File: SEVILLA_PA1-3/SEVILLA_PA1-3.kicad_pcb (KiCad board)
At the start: 2 copper layers, 64 x 46 mm, 10 parts, among them SW3 SW_SPST, SW4 SW_SPST, U1 HDSP-7401, U2 PIC16F84A-XXP, U3 HDSP-7401, Y1 4 MHz

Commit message: Refactor code structure and remove redundant sections for improved readability and maintainability
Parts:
- moved C2 44.5 mm to (161.0, 108.2), turned to 180 degrees
- moved U3 36.2 mm to (171.1, 91.0)
- moved U2 35.8 mm to (158.6, 101.6)
- moved U1 35.6 mm to (171.1, 105.6)
- moved SW4 33.1 mm to (118.5, 94.0)
- moved SW3 32.2 mm to (118.5, 80.0)
- moved R1 32.2 mm to (137.5, 77.5), turned to 90 degrees
- moved Y1 31.9 mm to (146.2, 83.5)
- moved R2 27.5 mm to (141.0, 98.0), turned to 180 degrees
- moved C1 22.3 mm to (146.0, 74.2)
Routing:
- net Net-(U1-F): track 41.6 -> 69.5 mm
- net GND: track 127.1 -> 152.1 mm
- net Net-(SW3-A): track 109.1 -> 88.9 mm
- net Net-(U1-E): track 61.3 -> 43.4 mm
- net Net-(U1-G): track 66.8 -> 49.3 mm
- net Net-(SW4-B): track 44.5 -> 59.4 mm
- net Net-(U2-RA3): track 55.0 -> 44.4 mm
- net Net-(U2-OSC2/CLKOUT): track 32.5 -> 24.9 mm
- net VCC: track 26.1 -> 19.5 mm
- net Net-(U1-C): track 27.0 -> 33.3 mm
- net Net-(U2-OSC1/CLKIN): track 30.8 -> 26.0 mm
- net Net-(U1-B): track 27.7 -> 24.1 mm
- net Net-(U2-TOCKI/RA4): track 26.7 -> 29.2 mm
- net Net-(U1-A): track 27.7 -> 25.4 mm
- net Net-(U1-D): track 31.9 -> 30.1 mm
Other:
- board size 64 x 46 mm -> 62 x 46 mm

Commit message: Refactor code structure for improved readability and maintainability
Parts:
- moved U1 1.76 mm to (171.5, 107.3)
- moved U2 1.76 mm to (159.0, 103.3)
- moved U3 1.76 mm to (171.5, 92.7)
- moved Y1 1.76 mm to (146.5, 85.2)
- moved SW3 1.76 mm to (118.9, 81.7)
- moved SW4 1.76 mm to (118.9, 95.7)
- moved C1 1.76 mm to (146.4, 75.9)
- moved C2 1.76 mm to (161.4, 110.0)
- moved R1 1.76 mm to (137.9, 79.2)
- moved R2 1.76 mm to (141.4, 99.7)
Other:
- board size 62 x 46 mm -> 100 x 50 mm
- board text removed: "100"
- board text removed: "20 pF"
- board text removed: "4 MHz"

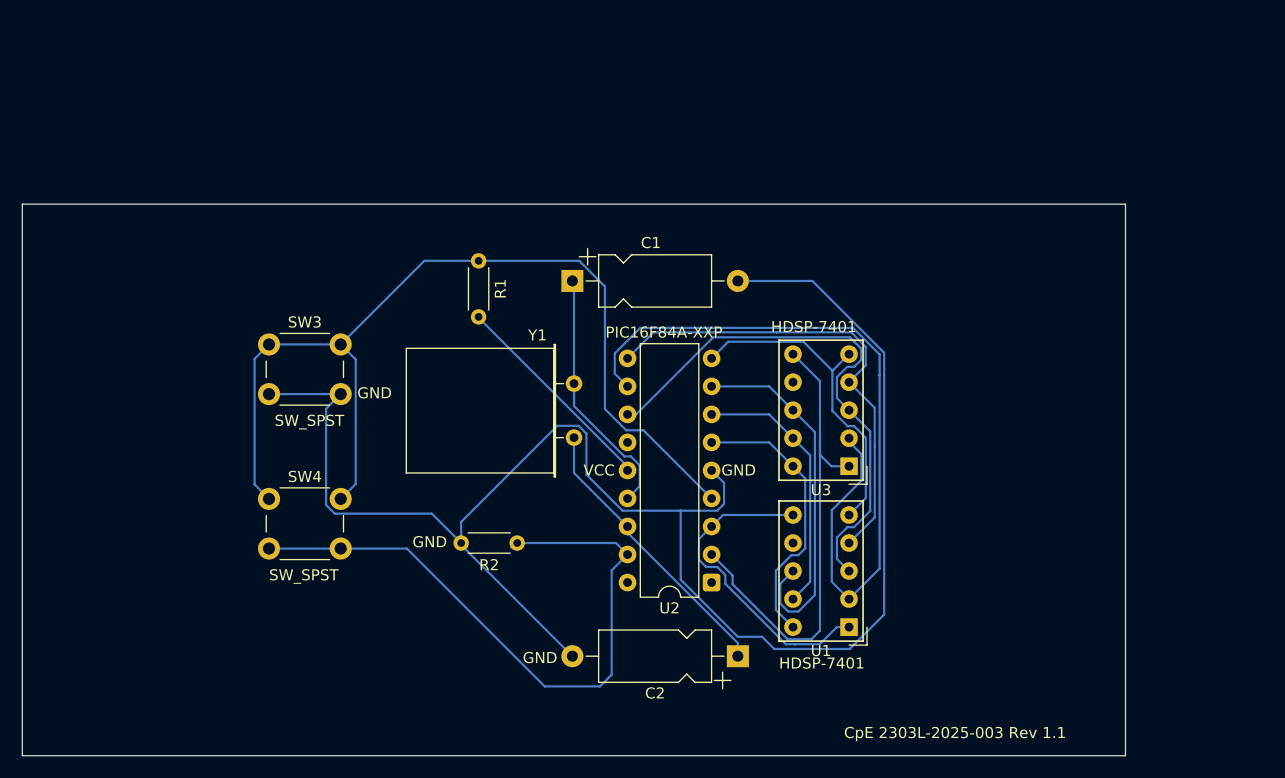
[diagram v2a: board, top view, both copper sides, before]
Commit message: Add lock file for PCB design with hostname and username information
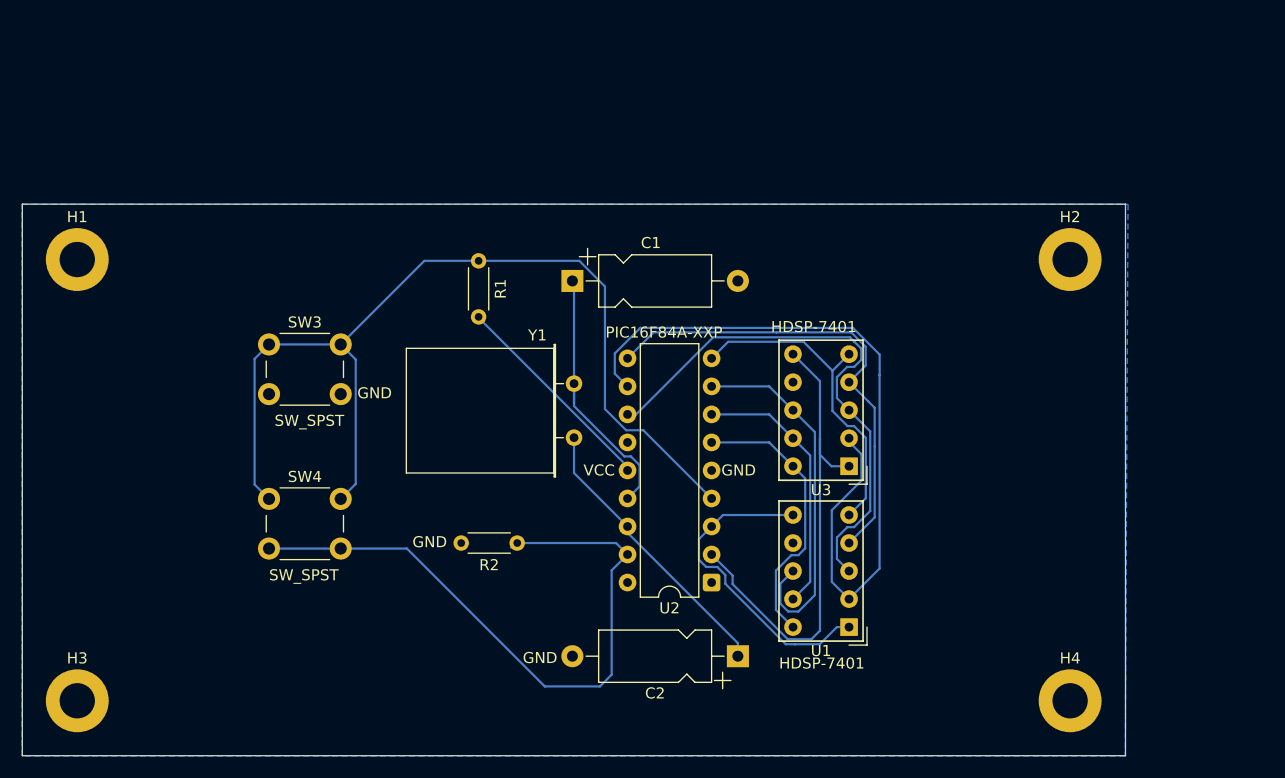
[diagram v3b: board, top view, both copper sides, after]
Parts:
- added H1: MountingHole, MountingHole:MountingHole_3.2mm_M3_ISO7380_Pad, F.Cu at (101.5, 74.0)
- added H2: MountingHole, MountingHole:MountingHole_3.2mm_M3_ISO7380_Pad, F.Cu at (191.5, 74.0)
- added H3: MountingHole, MountingHole:MountingHole_3.2mm_M3_ISO7380_Pad, F.Cu at (101.5, 114.0)
- added H4: MountingHole, MountingHole:MountingHole_3.2mm_M3_ISO7380_Pad, F.Cu at (191.5, 114.0)
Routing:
- net GND: track 152.1 -> 0.00 mm
- added copper zone on B.Cu, net GND
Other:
- board text added: "CpE 2303L-2025-003 Rev 1.2"
- board text removed: "CpE 2303L-2025-003 Rev 1.1"

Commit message: Refactor code structure for improved readability and maintainability
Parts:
- H1, H2, H3, H4: value MountingHole -> MountingHole_Pad
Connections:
- H1 pad 1: (no net) -> unconnected-(H1-Pad1)
- H2 pad 1: (no net) -> unconnected-(H2-Pad1)
- H3 pad 1: (no net) -> unconnected-(H3-Pad1)
- H4 pad 1: (no net) -> unconnected-(H4-Pad1)

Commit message: Refactor code structure and remove redundant sections for improved readability and maintainability
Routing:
- added copper zone on F.Cu, net GND
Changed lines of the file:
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@@
 		(net 1)
 		(net_name "GND")
-		(layer "B.Cu")
+		(layers "F.Cu" "B.Cu")
 		(hatch edge 0.5)
 		(connect_pads

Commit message: Refactor code structure and remove redundant sections for improved readability and maintainability
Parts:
- added J1: Conn_01x02, Connector_Molex:Molex_KK-254_AE-6410-02A_1x02_P2.54mm_Vertical, F.Cu at (143.6, 112.8)
- moved R2 47.0 mm to (185.8, 84.2), turned to -90 degrees
- moved C2 34.6 mm to (128.4, 99.6), turned to -90 degrees
- moved U1 33.0 mm to (146.6, 85.7), turned to 0 degrees
- moved U2 26.4 mm to (173.6, 81.3), turned to 0 degrees
- moved R1 26.4 mm to (140.8, 105.4)
- moved Y1 17.4 mm to (131.8, 94.5), turned to 180 degrees
- moved SW3 15.6 mm to (109.3, 94.1)
- moved SW4 15.4 mm to (109.3, 83.6)
- moved C1 14.9 mm to (131.6, 74.3)
- moved U3 12.9 mm to (160.0, 86.7), turned to 0 degrees
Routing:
- net Net-(U2-OSC1/CLKIN): track 26.0 -> 90.6 mm
- net Net-(U2-OSC2/CLKOUT): track 24.7 -> 74.4 mm
- net VCC: track 19.5 -> 61.4 mm
- net Net-(U1-G): track 49.3 -> 14.0 mm
- net Net-(U1-F): track 69.5 -> 39.2 mm
- net Net-(SW4-B): track 59.4 -> 87.5 mm
- net Net-(SW3-A): track 88.9 -> 104.0 mm
- net Net-(U2-TOCKI/RA4): track 29.2 -> 43.9 mm
- net Net-(U2-RA3): track 44.4 -> 30.0 mm
- net Net-(U1-C): track 33.3 -> 25.5 mm
- net Net-(U1-E): track 43.4 -> 38.2 mm
- net Net-(U1-B): track 24.1 -> 25.5 mm
- net Net-(U1-D): track 30.1 -> 29.5 mm
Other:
- board text removed: "VCC"

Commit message: Implement code changes to enhance functionality and improve performance
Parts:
- moved U1 15.9 mm to (155.0, 99.2)
- moved U3 7.68 mm to (155.4, 80.6)
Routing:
- net Net-(U1-F): track 39.2 -> 19.7 mm
- net Net-(SW3-A): track 104.0 -> 121.8 mm
- net Net-(U1-E): track 38.2 -> 55.2 mm
- net Net-(U1-G): track 14.0 -> 29.3 mm
- net Net-(U1-A): track 25.5 -> 39.4 mm
- net Net-(U1-D): track 29.5 -> 43.3 mm
- net Net-(U2-TOCKI/RA4): track 43.9 -> 32.4 mm
- net Net-(U1-C): track 25.5 -> 35.4 mm
- net Net-(U2-RA3): track 30.0 -> 20.8 mm
- net Net-(U2-OSC1/CLKIN): track 90.6 -> 98.7 mm
- net Net-(U1-B): track 25.5 -> 31.5 mm
- net VCC: track 61.4 -> 63.8 mm
- net Net-(U2-OSC2/CLKOUT): track 74.4 -> 75.0 mm

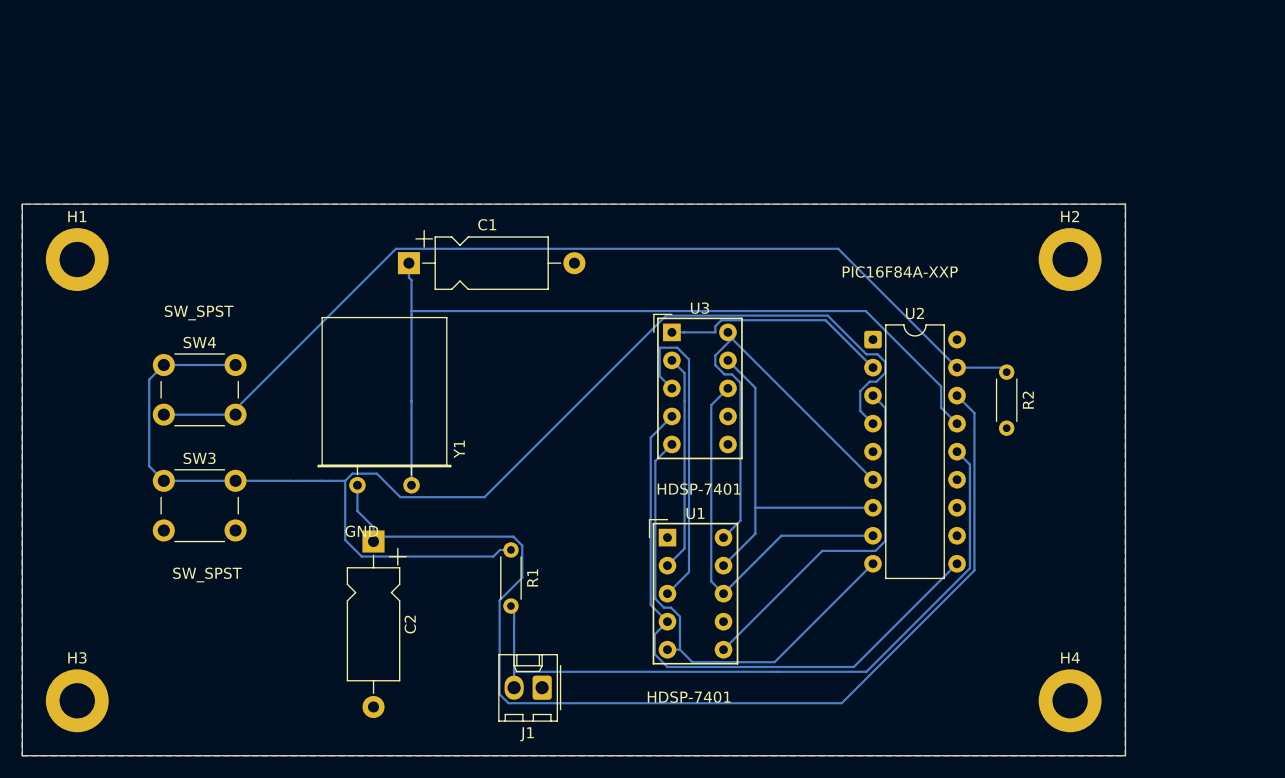
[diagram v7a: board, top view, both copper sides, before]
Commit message: Add initial freerouting rules for PCB design
- Introduced a new rules file for PCB freerouting with comprehensive settings.
- Configured autoroute settings including fanout, via costs, and layer rules for F.Cu and B.Cu.
- Defined clearance and width rules for traces and pads.
- Established padstack and via definitions for routing.
- Created default and kicad_default classes with associated nets and rules.
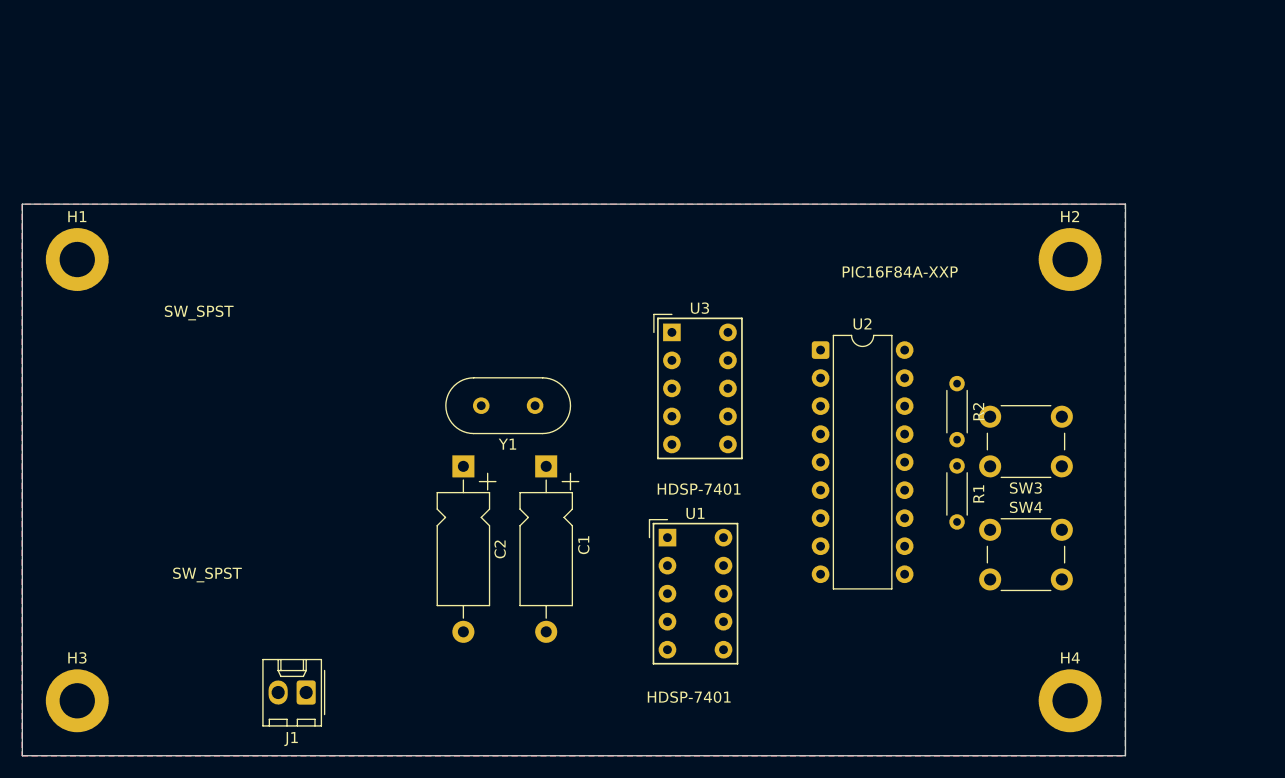
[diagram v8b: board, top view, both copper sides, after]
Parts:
- Y1: footprint Crystal:Crystal_HC49-U_Horizontal -> Crystal:Crystal_HC49-U_Vertical
- moved SW3 81.4 mm to (190.8, 92.8), turned to 180 degrees
- moved SW4 76.4 mm to (184.2, 98.5)
- moved R1 41.1 mm to (181.2, 97.8)
- moved C1 22.2 mm to (144.0, 92.8), turned to -90 degrees
- moved J1 21.4 mm to (122.2, 113.2)
- moved Y1 13.3 mm to (143.0, 87.2)
- moved C2 10.6 mm to (136.5, 92.8)
- moved U2 4.84 mm to (168.9, 82.2)
- moved R2 4.62 mm to (181.2, 85.2)
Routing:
- net Net-(SW3-A): track 121.8 -> 0.00 mm
- net Net-(U2-OSC1/CLKIN): track 98.7 -> 0.00 mm
- net Net-(SW4-B): track 87.5 -> 0.00 mm
- net Net-(U2-OSC2/CLKOUT): track 75.0 -> 0.00 mm
- net VCC: track 63.8 -> 0.00 mm
- net Net-(U1-E): track 55.2 -> 0.00 mm
- net Net-(U1-D): track 43.3 -> 0.00 mm
- net Net-(U1-A): track 39.4 -> 0.00 mm
- net Net-(U1-C): track 35.4 -> 0.00 mm
- net Net-(U2-TOCKI/RA4): track 32.4 -> 0.00 mm
- net Net-(U1-B): track 31.5 -> 0.00 mm
- net Net-(U1-G): track 29.3 -> 0.00 mm
- net Net-(U2-RA3): track 20.8 -> 0.00 mm
- net Net-(U1-F): track 19.7 -> 0.00 mm
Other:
- board text removed: "GND"
